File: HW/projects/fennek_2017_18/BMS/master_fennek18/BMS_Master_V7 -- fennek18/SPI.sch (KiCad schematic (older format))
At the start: 26 parts, among them Q2 BSS205N, U2 SN74HC138DR, U5 MAX3390EEUD

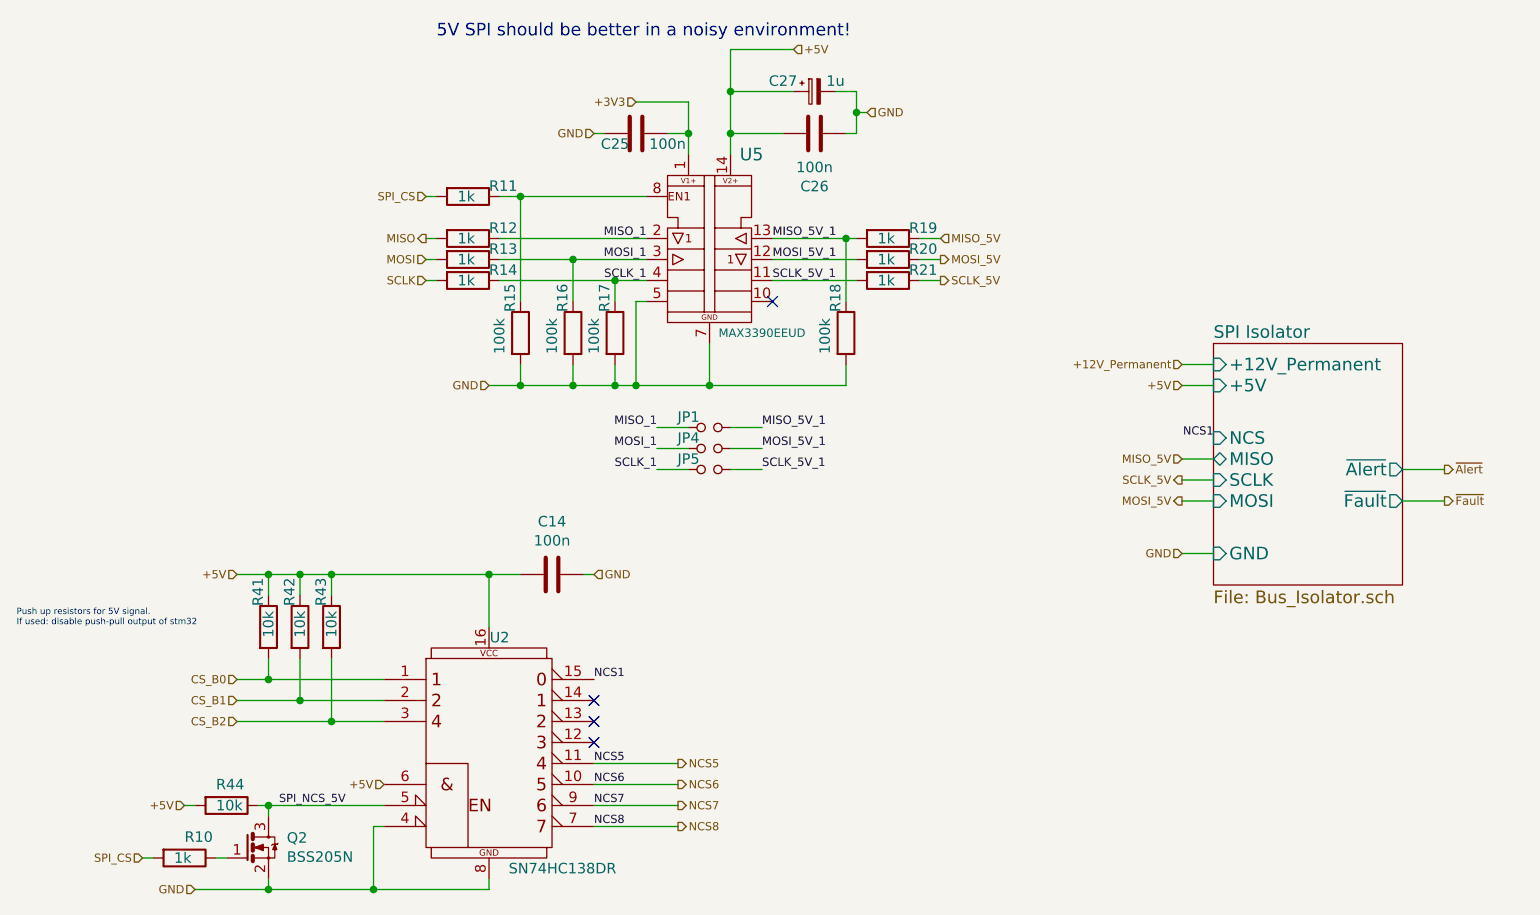
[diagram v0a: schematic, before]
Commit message: Update github repo with designs for fennek 2018
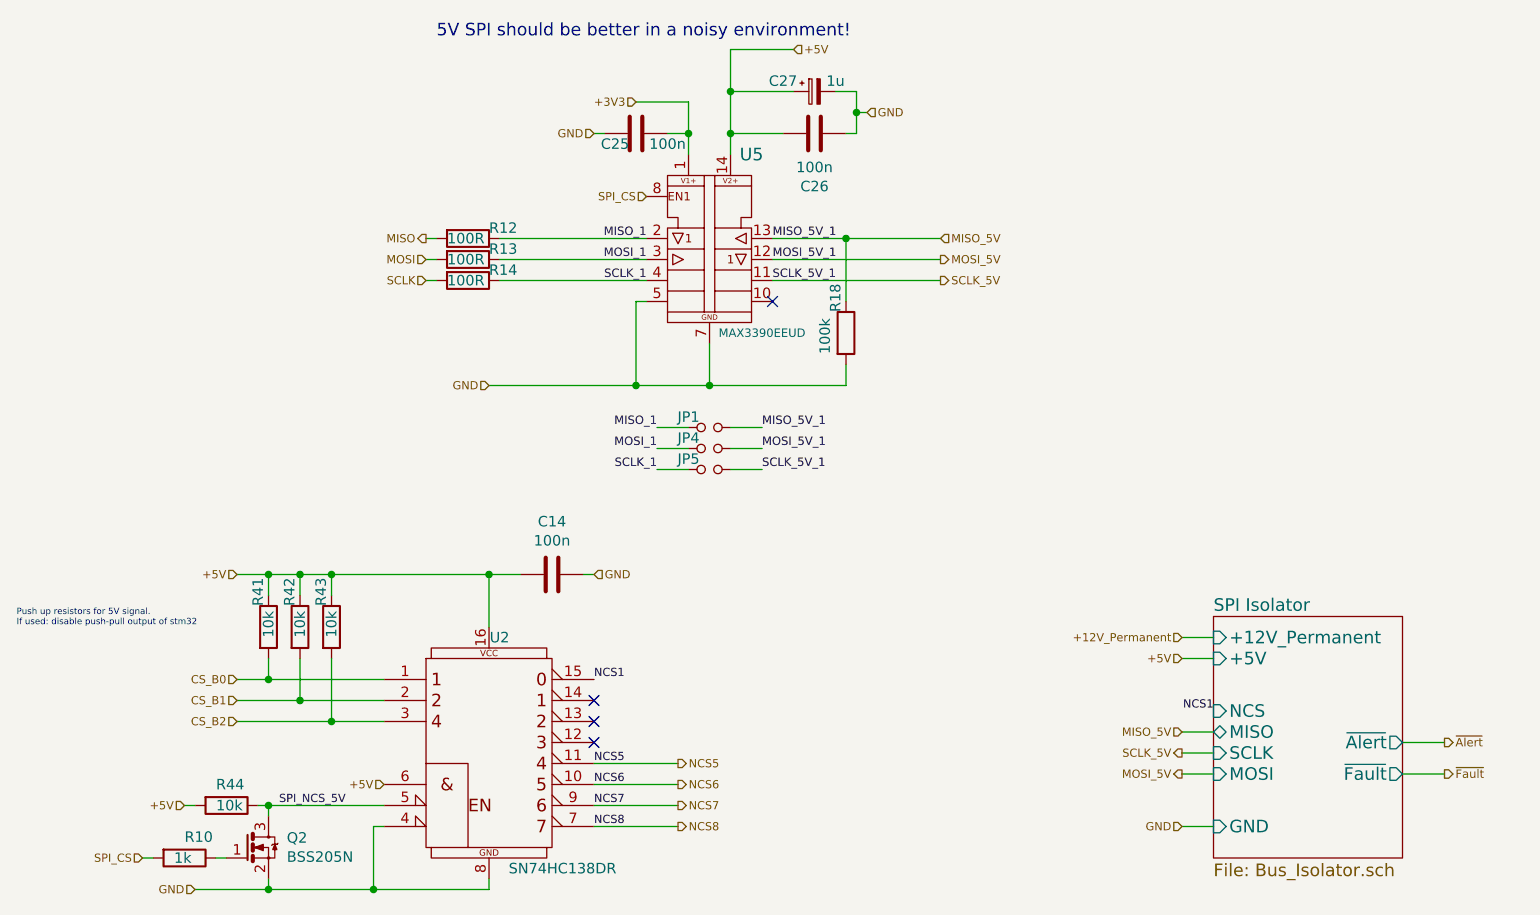
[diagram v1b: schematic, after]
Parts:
- removed R11, R19, R20, R21: 1k, tera_rlc:R_0603in, symbol R
- removed R15, R16, R17: 100k, tera_rlc:R_0603in, symbol R
- R12, R13, R14: value 1k -> 100R; HPN 11-1K00 -> 11-100R
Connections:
- net MISO_5V_1 is gone; now on net MISO_5V: JP1.2, R18.1, U5.13 (IN1)
- net MOSI_5V_1 is gone; now on net MOSI_5V: JP4.2, U5.12 (OUT2)
- net SCLK_5V_1 is gone; now on net SCLK_5V: JP5.2, U5.11 (OUT3)
- net SPI_CS: now also U5.8 (EN1)
